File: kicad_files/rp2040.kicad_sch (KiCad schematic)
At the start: 26 parts, among them J2 Conn_02x20_Counter_Clockwise, J3 Conn_01x03_Pin, Y1 Crystal_GND23

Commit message: header footprint generated
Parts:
- added IC3: W25Q128JVSIQ, SOIC127P790X216-8N, symbol SamacSys_Parts:W25Q128JVSIQ
- C? (x10): value C_Small -> 0.1uf
- J2: footprint (none) -> footprints:40Pin_Header
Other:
- note added: "Crystal"
- note added: "RP2040"
- note added: "SWD_CONNECTOR"
- moved on the sheet: C13, C14, R7, R8, Y1

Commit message: placement completed
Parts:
- removed IC3: W25Q128JVSIQ, SOIC127P790X216-8N, symbol SamacSys_Parts:W25Q128JVSIQ
- added C16: 100nf, Capacitor_SMD:C_0201_0603Metric, symbol Device:C_Small
- added C17: 2u2, Capacitor_SMD:C_0402_1005Metric, symbol Device:C_Small
- added C18: 1nf, Capacitor_SMD:C_0402_1005Metric, symbol Device:C_Small
- added IC3: W25Q16JVUXIQ_TR, SamacSys_Parts:SON50P300X200X60-9N, symbol SamacSys_Parts:W25Q16JVUXIQ_TR
- added Q1: DMG1012T-7, SamacSys_Parts:SOT50P160X80-3N, symbol SamacSys_Parts:DMG1012T-7
- added R12: 1K, Resistor_SMD:R_0201_0603Metric, symbol Device:R_Small
- added R13: DNP, Resistor_SMD:R_0201_0603Metric, symbol Device:R_Small
- added R14: 200K, Resistor_SMD:R_0201_0603Metric, symbol Device:R_Small
- added R15: 100K, Resistor_SMD:R_0201_0603Metric, symbol Device:R_Small
- added S1: PTS815_SJM_250_SMTR_LFS, SamacSys_Parts:PTS815SJM250SMTRLFS, symbol SamacSys_Parts:PTS815_SJM_250_SMTR_LFS
- added TP6: (no value), footprints:Custom_testpad, symbol Connector:TestPoint
- C13, C14, C15, C? (x10): footprint (none) -> Capacitor_SMD:C_0201_0603Metric
- D2: footprint (none) -> LED_SMD:LED_0402_1005Metric
- IC?: footprint QFN40P700X700X90-57N-D -> SamacSys_Parts:QFN40P700X700X90-57N-D
- J3: footprint (none) -> footprints:3Pin_Header
- R10, R11, R5, R6, R7, R8: footprint (none) -> Resistor_SMD:R_0201_0603Metric
- R9: footprint (none) -> Resistor_SMD:R_0402_1005Metric
- TP5: footprint (none) -> footprints:Custom_testpad
- Y1: footprint (none) -> SamacSys_Parts:YSX321SL
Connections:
- net IOVDD_1 is gone; now on net 3V3: C?.1, C?.1, C?.1, C?.1, C?.1, C?.1, C?.1, C?.1, C?.1, C?.1, IC?.1 (IOVDD_1), IC?.10 (IOVDD_2), IC?.22 (IOVDD_3), IC?.33 (IOVDD_4), IC?.42 (IOVDD_5), IC?.44 (VREG_VIN), IC?.48 (USB_VDD), IC?.49 (IOVDD_6)
- net 3V3: now also C16.1, C17.1, IC3.8 (VCC), Q1.1 (G), R13.2
- net GND: now also C?.2, C?.2, C?.2, C?.2, C?.2, C?.2, C?.2, C?.2, C?.2, C?.2, Y1.2, Y1.4, C16.2, C17.2, C18.2, IC3.4 (GND), R15.1, S1.3 (NO_1), S1.4 (NO_2)
- net GPIO29/ADC3: now also Q1.2 (S)
- net QSPI_SCLK: now also IC3.6 (CLK)
- net QSPI_SD0: now also IC3.5 (DI(IO0))
- net QSPI_SD1: now also IC3.2 (DO(IO1))
- net QSPI_SD2: now also IC3.3 (IO2)
- net QSPI_SD3: now also IC3.7 (IO3)
- net QSPI_SS_N: now also IC3.1 (~{CS}), R12.1, R13.1
- net VSYS: now also R14.2
- new net: R12.2, S1.1 (COM_1), S1.2 (COM_2), TP6.1
- new net: C18.1, Q1.3 (D), R14.1, R15.2
- no-connect marks 0 -> 1
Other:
- moved on the sheet: C13, C14, R7, R8, Y1

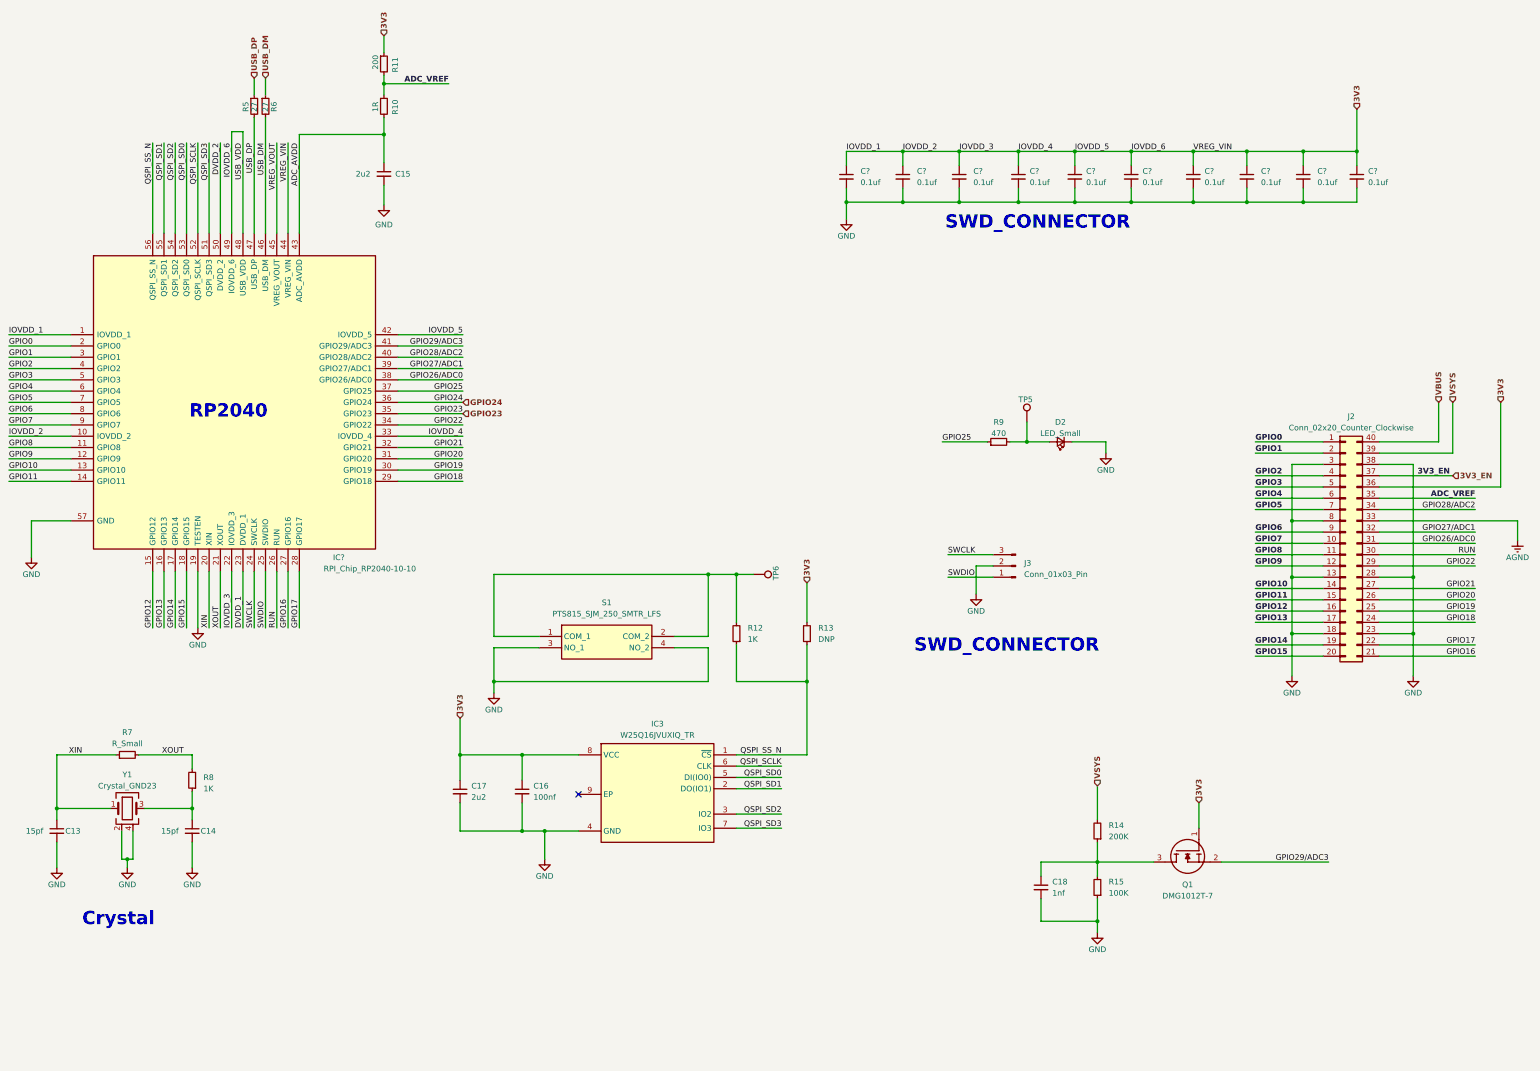
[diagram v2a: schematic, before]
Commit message: initial routing started
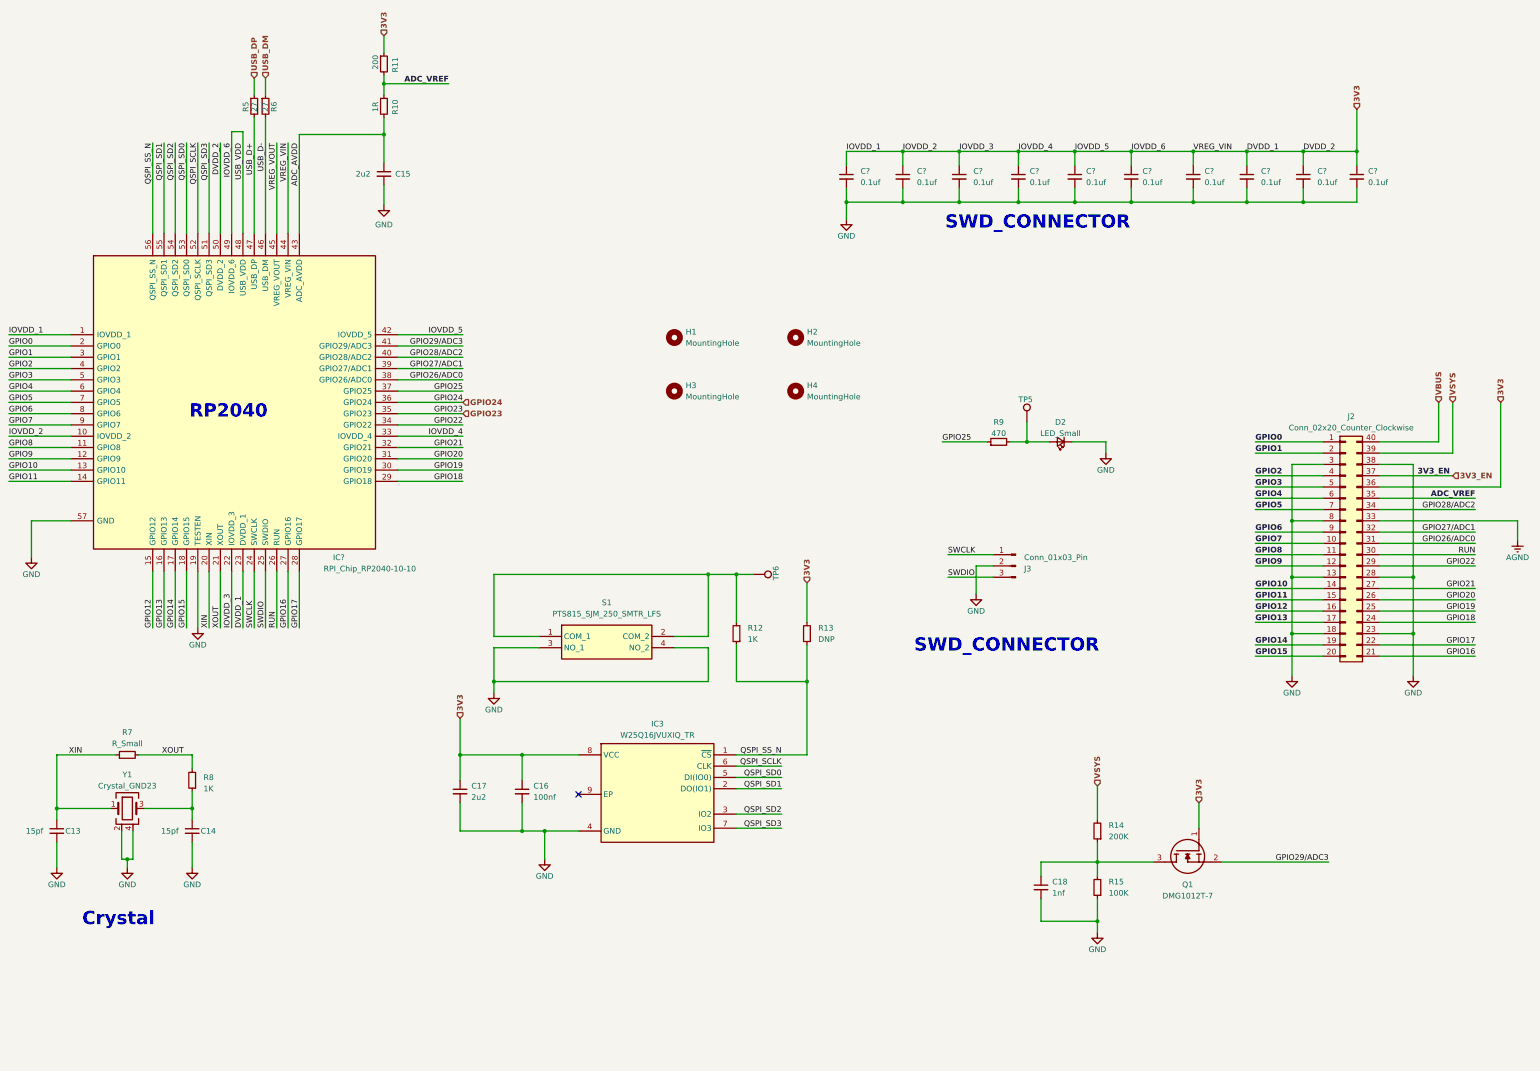
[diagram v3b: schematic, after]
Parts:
- added H1, H2, H3, H4: MountingHole, footprints:Mounting_Hole, symbol Mechanical:MountingHole
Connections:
- net DVDD_1 is gone; now on net 3V3: IC?.23 (DVDD_1)
- net DVDD_2 is gone; now on net 3V3: IC?.50 (DVDD_2)
- net SWCLK: now also J3.1 (Pin_1); no longer J3.3 (Pin_3)
- net SWDIO: now also J3.3 (Pin_3); no longer J3.1 (Pin_1)
- net USB_DM: no longer IC?.46 (USB_DM), R6.2
- net USB_DP: no longer IC?.47 (USB_DP), R5.2
- new net USB_D+: IC?.47 (USB_DP), R5.2
- new net USB_D-: IC?.46 (USB_DM), R6.2
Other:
- moved on the sheet: J3
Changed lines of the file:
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@@
     (effects (font (size 1.27 1.27)) (justify right bottom))
+  )
+  (label "DVDD_2" (at 330.835 48.26 0) (fields_autoplaced)
+    (effects (font (size 1.27 1.27)) (justify left bottom))
   )
   (label "GPIO3" (at 39.37 99.695 0) (fields_autoplaced)
@@
     (effects (font (size 1.27 1.27)) (justify right bottom))
   )
-  (label "USB_DP" (at 94.615 46.355 270) (fields_autoplaced)
+  (label "USB_D+" (at 94.615 46.355 270) (fields_autoplaced)
     (effects (font (size 1.27 1.27)) (justify right bottom))
   )
@@
     (effects (font (size 1.27 1.27)) (justify right bottom))
   )
-  (label "USB_DM" (at 97.155 46.355 270) (fields_autoplaced)
+  (label "USB_D-" (at 97.155 46.355 270) (fields_autoplaced)
     (effects (font (size 1.27 1.27)) (justify right bottom))
   )
@@
   (label "GPIO28{slash}ADC2" (at 141.605 94.615 180) (fields_autoplaced)
     (effects (font (size 1.27 1.27)) (justify right bottom))
+  )
+  (label "DVDD_1" (at 318.135 48.26 0) (fields_autoplaced)
+    (effects (font (size 1.27 1.27)) (justify left bottom))
   )
   (label "QSPI_SD3" (at 213.36 200.66 180) (fields_autoplaced)
@@
     (effects (font (size 1.27 1.27) bold) (justify left))
   )
+  (symbol (lib_id "Mechanical:MountingHole") (at 189.23 102.235 0) (unit 1)
+    (in_bom yes) (on_board yes) (dnp no) (fields_autoplaced)
+    (property "Reference" "H3" (at 191.77 100.965 0)
+      (effects (font (size 1.27 1.27)) (justify left))
+    )
+    (property "Value" "MountingHole" (at 191.77 103.505 0)
+      (effects (font (size 1.27 1.27)) (justify left))
+    )
+    (property "Footprint" "footprints:Mounting_Hole" (at 189.23 102.235 0)
+      (effects (font (size 1.27 1.27)) hide)
+    )
+    (property "Datasheet" "~" (at 189.23 102.235 0)
+      (effects (font (size 1.27 1.27)) hide)
+    )
+    (instances
+      (project "RP2040_Breakout"
+        (path "/bce568f8-09c9-431d-8eca-35cbbd37c7c1/0ca5b8d5-0466-420f-8a7d-f2250c18d4d6"
+          (reference "H3") (unit 1)
+        )
+      )
+    )
+  )
   (symbol (lib_id "Device:C_Small") (at 227.965 53.975 0) (unit 1)
     (in_bom yes) (on_board yes) (dnp no) (fields_autoplaced)
@@
         (path "/bce568f8-09c9-431d-8eca-35cbbd37c7c1/0ca5b8d5-0466-420f-8a7d-f2250c18d4d6"
           (reference "C1") (unit 1)
+        )
+      )
+    )
+  )
+  (symbol (lib_id "Mechanical:MountingHole") (at 216.535 90.17 0) (unit 1)
+    (in_bom yes) (on_board yes) (dnp no) (fields_autoplaced)
+    (property "Reference" "H2" (at 219.075 88.9 0)
+      (effects (font (size 1.27 1.27)) (justify left))
+    )
+    (property "Value" "MountingHole" (at 219.075 91.44 0)
+      (effects (font (size 1.27 1.27)) (justify left))
+    )
+    (property "Footprint" "footprints:Mounting_Hole" (at 216.535 90.17 0)
+      (effects (font (size 1.27 1.27)) hide)
+    )
+    (property "Datasheet" "~" (at 216.535 90.17 0)
+      (effects (font (size 1.27 1.27)) hide)
+    )
+    (instances
+      (project "RP2040_Breakout"
+        (path "/bce568f8-09c9-431d-8eca-35cbbd37c7c1/0ca5b8d5-0466-420f-8a7d-f2250c18d4d6"
+          (reference "H2") (unit 1)
         )
       )
@@
     )
   )
-  (symbol (lib_id "Connector:Conn_01x03_Pin") (at 266.065 141.605 180) (unit 1)
-    (in_bom yes) (on_board yes) (dnp no) (fields_autoplaced)
-    (property "Reference" "J3" (at 267.97 140.97 0)
+  (symbol (lib_id "Connector:Conn_01x03_Pin") (at 266.065 141.605 0) (mirror y) (unit 1)
+    (in_bom yes) (on_board yes) (dnp no)
+    (property "Reference" "J3" (at 267.97 142.24 0)
       (effects (font (size 1.27 1.27)) (justify right))
     )
-    (property "Value" "Conn_01x03_Pin" (at 267.97 143.51 0)
+    (property "Value" "Conn_01x03_Pin" (at 267.97 139.7 0)
       (effects (font (size 1.27 1.27)) (justify right))
     )
@@
     )
   )
+  (symbol (lib_id "Mechanical:MountingHole") (at 216.535 102.235 0) (unit 1)
+    (in_bom yes) (on_board yes) (dnp no) (fields_autoplaced)
+    (property "Reference" "H4" (at 219.075 100.965 0)
+      (effects (font (size 1.27 1.27)) (justify left))
+    )
+    (property "Value" "MountingHole" (at 219.075 103.505 0)
+      (effects (font (size 1.27 1.27)) (justify left))
+    )
+    (property "Footprint" "footprints:Mounting_Hole" (at 216.535 102.235 0)
+      (effects (font (size 1.27 1.27)) hide)
+    )
+    (property "Datasheet" "~" (at 216.535 102.235 0)
+      (effects (font (size 1.27 1.27)) hide)
+    )
+    (instances
+      (project "RP2040_Breakout"
+        (path "/bce568f8-09c9-431d-8eca-35cbbd37c7c1/0ca5b8d5-0466-420f-8a7d-f2250c18d4d6"
+          (reference "H4") (unit 1)
+        )
+      )
+    )
+  )
   (symbol (lib_id "Device:C_Small") (at 140.97 192.405 0) (mirror y) (unit 1)
     (in_bom yes) (on_board yes) (dnp no) (fields_autoplaced)
@@
         )
       )
+    )
+  )
+  (symbol (lib_id "Mechanical:MountingHole") (at 189.23 90.17 0) (unit 1)
+    (in_bom yes) (on_board yes) (dnp no) (fields_autoplaced)
+    (property "Reference" "H1" (at 191.77 88.9 0)
+      (effects (font (size 1.27 1.27)) (justify left))
+    )
+    (property "Value" "MountingHole" (at 191.77 91.44 0)
+      (effects (font (size 1.27 1.27)) (justify left))
+    )
+    (property "Footprint" "footprints:Mounting_Hole" (at 189.23 90.17 0)
+      (effects (font (size 1.27 1.27)) hide)
+    )
+    (property "Datasheet" "~" (at 189.23 90.17 0)
+      (effects (font (size 1.27 1.27)) hide)
+    )
+    (instances
+      (project "RP2040_Breakout"
+        (path "/bce568f8-09c9-431d-8eca-35cbbd37c7c1/0ca5b8d5-0466-420f-8a7d-f2250c18d4d6"
+          (reference "H1") (unit 1)
+        )
+      )
